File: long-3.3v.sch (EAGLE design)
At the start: 20 parts, among them U1 USD-SOCKET, U2 MCP73831, U4 ADXL375BCCZ, X1 Micro USB

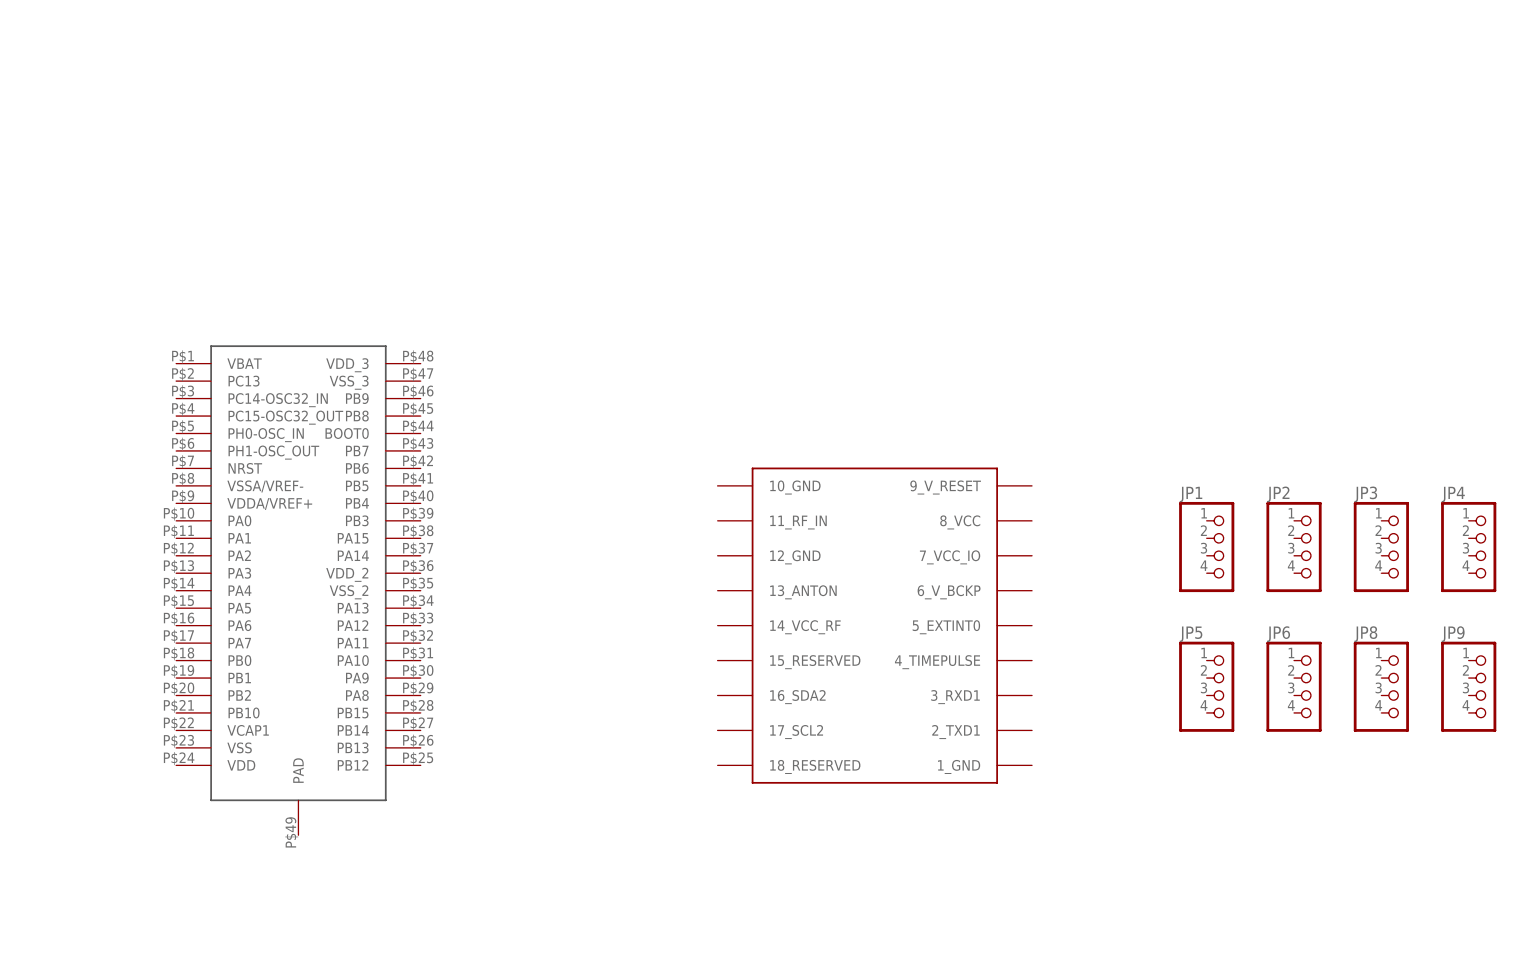
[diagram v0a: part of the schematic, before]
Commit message: Added RFM69HW and more stuff
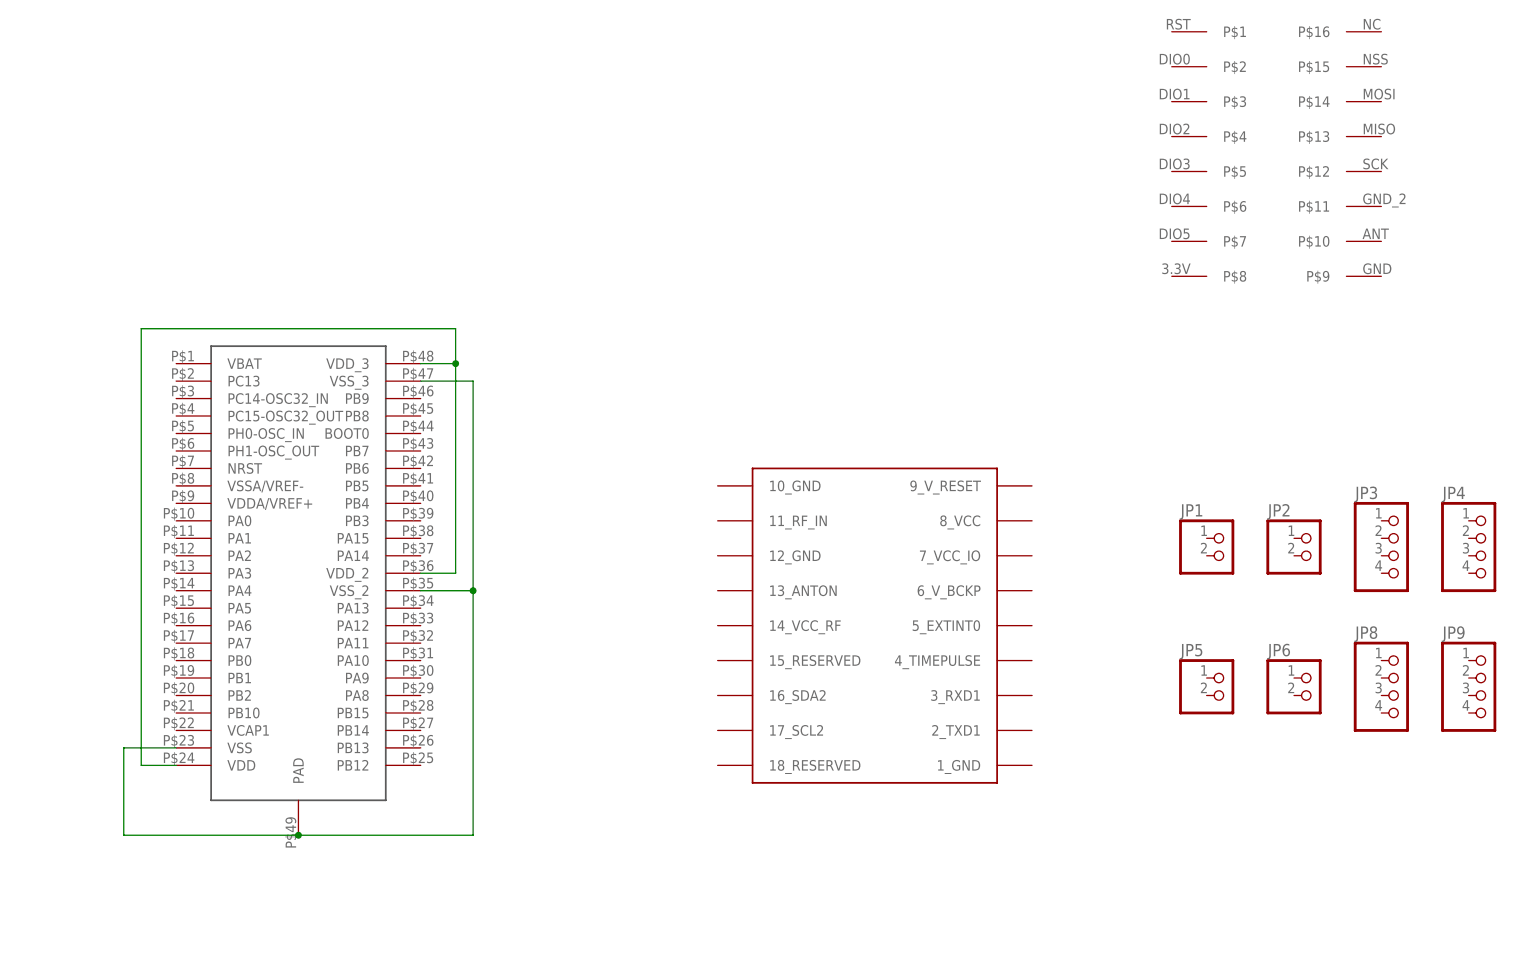
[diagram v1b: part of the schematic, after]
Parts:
- added U$3: RFM69HW, RFM69HW:RFM69HW
- JP1, JP2, JP5, JP6: device pinhead:PINHD-1X4 -> pinhead:PINHD-1X2
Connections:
- new net N$1: U$1.VDD, U$1.VDD_2, U$1.VDD_3
- new net N$2: U$1.PAD, U$1.VSS, U$1.VSS_2, U$1.VSS_3
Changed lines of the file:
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@@
 <part name="X1" library="SparkFun" deviceset="USB" device="-MICROB" value="Micro USB"/>
 <part name="U$2" library="Ava" deviceset="UBLOX_MAX" device=""/>
-<part name="JP1" library="pinhead" deviceset="PINHD-1X4" device=""/>
-<part name="JP2" library="pinhead" deviceset="PINHD-1X4" device=""/>
+<part name="JP1" library="pinhead" deviceset="PINHD-1X2" device=""/>
+<part name="JP2" library="pinhead" deviceset="PINHD-1X2" device=""/>
 <part name="JP3" library="pinhead" deviceset="PINHD-1X4" device=""/>
 <part name="JP4" library="pinhead" deviceset="PINHD-1X4" device=""/>
-<part name="JP5" library="pinhead" deviceset="PINHD-1X4" device=""/>
-<part name="JP6" library="pinhead" deviceset="PINHD-1X4" device=""/>
+<part name="JP5" library="pinhead" deviceset="PINHD-1X2" device=""/>
+<part name="JP6" library="pinhead" deviceset="PINHD-1X2" device=""/>
 <part name="JP8" library="pinhead" deviceset="PINHD-1X4" device=""/>
 <part name="JP9" library="pinhead" deviceset="PINHD-1X4" device=""/>
 <part name="U4" library="adxl375bccz" deviceset="ADXL375BCCZ" device=""/>
 <part name="U$1" library="STM32F411CEU6" deviceset="STM32F411CEU6" device=""/>
+<part name="U$3" library="RFM69HW" deviceset="RFM69HW" device=""/>
 </parts>
 <sheets>
@@
 <instance part="X1" gate="G$1" x="66.04" y="43.18" rot="MR0"/>
 <instance part="U$2" gate="G$1" x="187.96" y="119.38"/>
-<instance part="JP1" gate="A" x="238.76" y="124.46"/>
-<instance part="JP2" gate="A" x="251.46" y="124.46"/>
+<instance part="JP1" gate="G$1" x="238.76" y="124.46"/>
+<instance part="JP2" gate="G$1" x="251.46" y="124.46"/>
 <instance part="JP3" gate="A" x="264.16" y="124.46"/>
 <instance part="JP4" gate="A" x="276.86" y="124.46"/>
-<instance part="JP5" gate="A" x="238.76" y="104.14"/>
-<instance part="JP6" gate="A" x="251.46" y="104.14"/>
+<instance part="JP5" gate="G$1" x="238.76" y="104.14"/>
+<instance part="JP6" gate="G$1" x="251.46" y="104.14"/>
 <instance part="JP8" gate="A" x="264.16" y="104.14"/>
 <instance part="JP9" gate="A" x="276.86" y="104.14"/>
 <instance part="U4" gate="A" x="322.58" y="119.38"/>
 <instance part="U$1" gate="G$1" x="106.68" y="132.08"/>
+<instance part="U$3" gate="G$1" x="246.38" y="182.88"/>
 </instances>
 <busses>
@@
 </segment>
 </net>
+<net name="N$1" class="0">
+<segment>
+<pinref part="U$1" gate="G$1" pin="VDD"/>
+<wire x1="86.36" y1="93.98" x2="81.28" y2="93.98" width="0.1524" layer="91"/>
+<wire x1="81.28" y1="93.98" x2="81.28" y2="157.48" width="0.1524" layer="91"/>
+<wire x1="81.28" y1="157.48" x2="127" y2="157.48" width="0.1524" layer="91"/>
+<wire x1="127" y1="157.48" x2="127" y2="152.4" width="0.1524" layer="91"/>
+<pinref part="U$1" gate="G$1" pin="VDD_3"/>
+<wire x1="127" y1="152.4" x2="121.92" y2="152.4" width="0.1524" layer="91"/>
+<wire x1="127" y1="152.4" x2="127" y2="121.92" width="0.1524" layer="91"/>
+<pinref part="U$1" gate="G$1" pin="VDD_2"/>
+<wire x1="127" y1="121.92" x2="121.92" y2="121.92" width="0.1524" layer="91"/>
+<junction x="127" y="152.4"/>
+</segment>
+</net>
+<net name="N$2" class="0">
+<segment>
+<pinref part="U$1" gate="G$1" pin="VSS"/>
+<wire x1="86.36" y1="96.52" x2="78.74" y2="96.52" width="0.1524" layer="91"/>
+<wire x1="78.74" y1="96.52" x2="78.74" y2="83.82" width="0.1524" layer="91"/>
+<wire x1="78.74" y1="83.82" x2="104.14" y2="83.82" width="0.1524" layer="91"/>
+<wire x1="104.14" y1="83.82" x2="129.54" y2="83.82" width="0.1524" layer="91"/>
+<wire x1="129.54" y1="83.82" x2="129.54" y2="119.38" width="0.1524" layer="91"/>
+<pinref part="U$1" gate="G$1" pin="VSS_2"/>
+<wire x1="129.54" y1="119.38" x2="121.92" y2="119.38" width="0.1524" layer="91"/>
+<wire x1="129.54" y1="119.38" x2="129.54" y2="149.86" width="0.1524" layer="91"/>
+<pinref part="U$1" gate="G$1" pin="VSS_3"/>
+<wire x1="129.54" y1="149.86" x2="121.92" y2="149.86" width="0.1524" layer="91"/>
+<pinref part="U$1" gate="G$1" pin="PAD"/>
+<junction x="104.14" y="83.82"/>
+<junction x="129.54" y="119.38"/>
+</segment>
+</net>

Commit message: Updated schematic, connected peripherals
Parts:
- added IC1: (no value), v-reg:XC63FPM
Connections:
- removed net N$1: U$1.VDD, U$1.VDD_2, U$1.VDD_3
- removed net N$2: U$1.PAD, U$1.VSS, U$1.VSS_2, U$1.VSS_3
- new net FC_RX: U$1.PA10
- new net FC_TX: U$1.PA9
- new net GPS_RX: U$2.3_RXD1
- new net GPS_TX: U$2.2_TXD1
- new net RADIO_CS: U$1.PB12, U$3.P$15
- new net RADIO_MISO: U$1.PB14, U$3.P$13
- new net RADIO_MOSI: U$1.PB15, U$3.P$14
- new net RADIO_SCK: U$1.PB13, U$3.P$12
- new net SCL: U$1.PB6, U4.SCL/SCLK
- new net SDA: U$1.PB7, U4.SDA/SDI/SDIO
- new net SD_CS: U$1.PA4, U1.CS
- new net SD_MISO: U$1.PA6, U1.DO
- new net SD_MOSI: U$1.PA7, U1.DI
- new net SD_SCK: U$1.PA5, U1.SCK
- new net VCC: IC1.OUT, U$1.VDD, U$1.VDD_2, U$1.VDD_3, U$2.14_VCC_RF, U$2.6_V_BCKP, U$2.7_VCC_IO, U$2.8_VCC, U$2.9_V_RESET, U$3.P$8, U1.VCC, U4.VDD_I/O, U4.VS
- net GND: now also IC1.GND, U$1.PAD, U$1.VSS, U$1.VSS_2, U$1.VSS_3, U$2.10_GND, U$2.12_GND, U$2.1_GND, U$3.P$11, U$3.P$9, U1.GND, U1.SHIELD@1, U1.SHIELD@3, U4.GND, U4.GND_2, U4.GND_3
- net VBAT: now also IC1.IN
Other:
- moved on the sheet: C3, C4, D11, JP7, R3, R4, U1, U2, U4
